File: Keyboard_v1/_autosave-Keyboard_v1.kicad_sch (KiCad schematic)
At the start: 16 parts, among them SW1 SW_Push, U1 ATmega32U4-A, Y1 16MHz

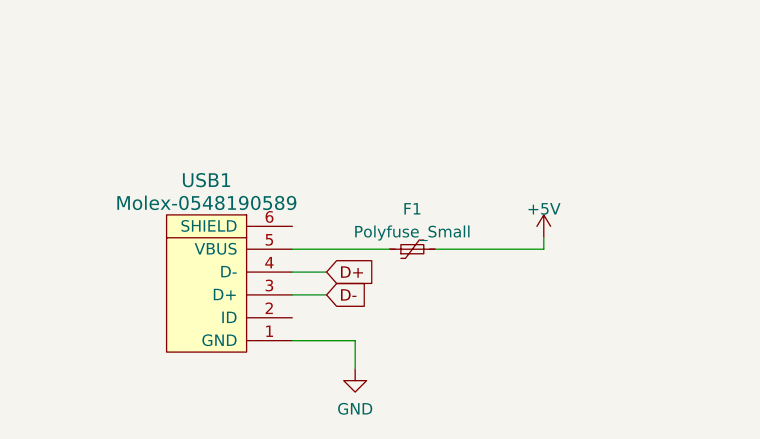
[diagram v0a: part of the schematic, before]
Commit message: routed MCU and key rows
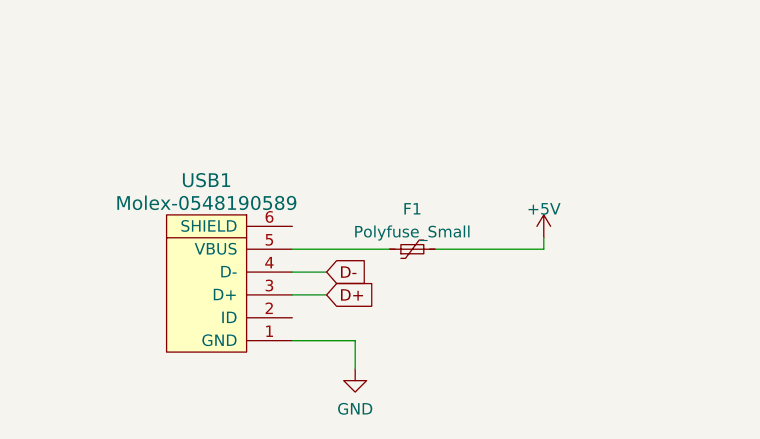
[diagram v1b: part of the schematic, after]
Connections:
- net D+: now also USB1.3 (D+); no longer USB1.4 (D-)
- net D-: now also USB1.4 (D-); no longer USB1.3 (D+)
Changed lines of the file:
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@@
     (effects (font (size 1.27 1.27)) (justify left bottom))
   )
-  (global_label "D+" (shape input) (at 70.485 148.59 0) (fields_autoplaced)
+  (global_label "D+" (shape input) (at 70.485 151.13 0) (fields_autoplaced)
     (effects (font (size 1.27 1.27)) (justify left))
-    (property "Intersheetrefs" "${INTERSHEET_REFS}" (at 76.2332 148.59 0)
+    (property "Intersheetrefs" "${INTERSHEET_REFS}" (at 76.2332 151.13 0)
       (effects (font (size 1.27 1.27)) (justify left) hide)
     )
   )
-  (global_label "D-" (shape input) (at 107.315 78.74 180) (fields_autoplaced)
-    (effects (font (size 1.27 1.27)) (justify right))
-    (property "Intersheetrefs" "${INTERSHEET_REFS}" (at 101.5668 78.74 0)
-      (effects (font (size 1.27 1.27)) (justify right) hide)
-    )
-  )
-  (global_label "D-" (shape input) (at 70.485 151.13 0) (fields_autoplaced)
+  (global_label "D-" (shape input) (at 70.485 148.59 0) (fields_autoplaced)
     (effects (font (size 1.27 1.27)) (justify left))
-    (property "Intersheetrefs" "${INTERSHEET_REFS}" (at 76.2332 151.13 0)
+    (property "Intersheetrefs" "${INTERSHEET_REFS}" (at 76.2332 148.59 0)
       (effects (font (size 1.27 1.27)) (justify left) hide)
     )
@@
       (effects (font (size 1.27 1.27)) (justify right) hide)
     )
+  )
+  (global_label "D-" (shape input) (at 107.315 78.74 180) (fields_autoplaced)
+    (effects (font (size 1.27 1.27)) (justify right))
+    (property "Intersheetrefs" "${INTERSHEET_REFS}" (at 101.5668 78.74 0)
+      (effects (font (size 1.27 1.27)) (justify right) hide)
+    )

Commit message: all rows and cols connected to MCU
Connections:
- net ROW2: now reaches U1.10 (PB2)
- net ROW3: now reaches U1.11 (PB3)
- net COL13: now reaches U1.18 (PD0)
- net COL12: now reaches U1.19 (PD1)
- net ROW4: now reaches U1.20 (PD2)
- net ROW5: now reaches U1.21 (PD3)
- net COL11: now reaches U1.22 (PD5)
- net COL3: now reaches U1.25 (PD4)
- net COL4: now reaches U1.26 (PD6)
- net COL5: now reaches U1.27 (PD7)
- net COL6: now reaches U1.28 (PB4)
- net COL7: now reaches U1.29 (PB5)
- net COL8: now reaches U1.30 (PB6)
- net COL9: now reaches U1.31 (PC6)
- net COL10: now reaches U1.32 (PC7)
- net COL0: now reaches U1.38 (PF5)
- net COL1: now reaches U1.39 (PF4)
- net COL2: now reaches U1.40 (PF1)
- net ROW0: now reaches U1.8 (PB0)
- net ROW1: now reaches U1.9 (PB1)
- no-connect marks 26 -> 6
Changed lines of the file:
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@@
   (junction (at 125.095 60.96) (diameter 0) (color 0 0 0 0)
   )
-  (no_connect (at 175.26 83.82))
   (no_connect (at 175.26 106.68))
   (no_connect (at 144.78 66.04))
-  (no_connect (at 175.26 66.04))
-  (no_connect (at 175.26 96.52))
-  (no_connect (at 175.26 63.5))
   (no_connect (at 175.26 121.92))
-  (no_connect (at 175.26 99.06))
-  (no_connect (at 175.26 116.84))
-  (no_connect (at 175.26 50.8))
-  (no_connect (at 175.26 119.38))
-  (no_connect (at 175.26 58.42))
-  (no_connect (at 175.26 55.88))
-  (no_connect (at 175.26 114.3))
-  (no_connect (at 175.26 53.34))
-  (no_connect (at 175.26 73.66))
-  (no_connect (at 175.26 93.98))
-  (no_connect (at 175.26 81.28))
-  (no_connect (at 175.26 86.36))
   (no_connect (at 175.26 111.76))
-  (no_connect (at 175.26 60.96))
   (no_connect (at 175.26 124.46))
   (no_connect (at 175.26 68.58))
-  (no_connect (at 175.26 88.9))
-  (no_connect (at 175.26 91.44))
-  (no_connect (at 175.26 76.2))
   (wire (pts (xy 162.56 41.91) (xy 162.56 43.18))
     (stroke (width 0) (type default))
@@
     (stroke (width 0) (type default))
   )
-  (wire (pts (xy 182.88 104.14) (xy 182.88 112.395))
+  (wire (pts (xy 183.515 104.14) (xy 183.515 106.045))
     (stroke (width 0) (type default))
   )
@@
     (stroke (width 0) (type default))
   )
-  (wire (pts (xy 181.61 104.14) (xy 182.88 104.14))
+  (wire (pts (xy 181.61 104.14) (xy 183.515 104.14))
     (stroke (width 0) (type default))
   )
@@
     (effects (font (size 1.27 1.27)) (justify left bottom))
   )
+  (global_label "COL4" (shape input) (at 175.26 96.52 0) (fields_autoplaced)
+    (effects (font (size 1.27 1.27)) (justify left))
+    (property "Intersheetrefs" "${INTERSHEET_REFS}" (at 183.0039 96.52 0)
+      (effects (font (size 1.27 1.27)) (justify left) hide)
+    )
+  )
+  (global_label "COL0" (shape input) (at 175.26 119.38 0) (fields_autoplaced)
+    (effects (font (size 1.27 1.27)) (justify left))
+    (property "Intersheetrefs" "${INTERSHEET_REFS}" (at 183.0039 119.38 0)
+      (effects (font (size 1.27 1.27)) (justify left) hide)
+    )
+  )
+  (global_label "COL8" (shape input) (at 175.26 66.04 0) (fields_autoplaced)
+    (effects (font (size 1.27 1.27)) (justify left))
+    (property "Intersheetrefs" "${INTERSHEET_REFS}" (at 183.0039 66.04 0)
+      (effects (font (size 1.27 1.27)) (justify left) hide)
+    )
+  )
+  (global_label "COL10" (shape input) (at 175.26 76.2 0) (fields_autoplaced)
+    (effects (font (size 1.27 1.27)) (justify left))
+    (property "Intersheetrefs" "${INTERSHEET_REFS}" (at 184.2134 76.2 0)
+      (effects (font (size 1.27 1.27)) (justify left) hide)
+    )
+  )
   (global_label "D+" (shape input) (at 70.485 151.13 0) (fields_autoplaced)
     (effects (font (size 1.27 1.27)) (justify left))
@@
     )
   )
+  (global_label "COL12" (shape input) (at 175.26 83.82 0) (fields_autoplaced)
+    (effects (font (size 1.27 1.27)) (justify left))
+    (property "Intersheetrefs" "${INTERSHEET_REFS}" (at 184.2134 83.82 0)
+      (effects (font (size 1.27 1.27)) (justify left) hide)
+    )
+  )
+  (global_label "COL5" (shape input) (at 175.26 99.06 0) (fields_autoplaced)
+    (effects (font (size 1.27 1.27)) (justify left))
+    (property "Intersheetrefs" "${INTERSHEET_REFS}" (at 183.0039 99.06 0)
+      (effects (font (size 1.27 1.27)) (justify left) hide)
+    )
+  )
   (global_label "D-" (shape input) (at 70.485 148.59 0) (fields_autoplaced)
     (effects (font (size 1.27 1.27)) (justify left))
     (property "Intersheetrefs" "${INTERSHEET_REFS}" (at 76.2332 148.59 0)
+      (effects (font (size 1.27 1.27)) (justify left) hide)
+    )
+  )
+  (global_label "ROW0" (shape input) (at 175.26 50.8 0) (fields_autoplaced)
+    (effects (font (size 1.27 1.27)) (justify left))
+    (property "Intersheetrefs" "${INTERSHEET_REFS}" (at 183.4272 50.8 0)
+      (effects (font (size 1.27 1.27)) (justify left) hide)
+    )
+  )
+  (global_label "COL7" (shape input) (at 175.26 63.5 0) (fields_autoplaced)
+    (effects (font (size 1.27 1.27)) (justify left))
+    (property "Intersheetrefs" "${INTERSHEET_REFS}" (at 183.0039 63.5 0)
+      (effects (font (size 1.27 1.27)) (justify left) hide)
+    )
+  )
+  (global_label "ROW2" (shape input) (at 175.26 55.88 0) (fields_autoplaced)
+    (effects (font (size 1.27 1.27)) (justify left))
+    (property "Intersheetrefs" "${INTERSHEET_REFS}" (at 183.4272 55.88 0)
+      (effects (font (size 1.27 1.27)) (justify left) hide)
+    )
+  )
+  (global_label "ROW4" (shape input) (at 175.26 86.36 0) (fields_autoplaced)
+    (effects (font (size 1.27 1.27)) (justify left))
+    (property "Intersheetrefs" "${INTERSHEET_REFS}" (at 183.4272 86.36 0)
+      (effects (font (size 1.27 1.27)) (justify left) hide)
+    )
+  )
+  (global_label "COL13" (shape input) (at 175.26 81.28 0) (fields_autoplaced)
+    (effects (font (size 1.27 1.27)) (justify left))
+    (property "Intersheetrefs" "${INTERSHEET_REFS}" (at 184.2134 81.28 0)
+      (effects (font (size 1.27 1.27)) (justify left) hide)
+    )
+  )
+  (global_label "COL1" (shape input) (at 175.26 116.84 0) (fields_autoplaced)
+    (effects (font (size 1.27 1.27)) (justify left))
+    (property "Intersheetrefs" "${INTERSHEET_REFS}" (at 183.0039 116.84 0)
+      (effects (font (size 1.27 1.27)) (justify left) hide)
+    )
+  )
+  (global_label "COL9" (shape input) (at 175.26 73.66 0) (fields_autoplaced)
+    (effects (font (size 1.27 1.27)) (justify left))
+    (property "Intersheetrefs" "${INTERSHEET_REFS}" (at 183.0039 73.66 0)
+      (effects (font (size 1.27 1.27)) (justify left) hide)
+    )
+  )
+  (global_label "COL3" (shape input) (at 175.26 91.44 0) (fields_autoplaced)
+    (effects (font (size 1.27 1.27)) (justify left))
+    (property "Intersheetrefs" "${INTERSHEET_REFS}" (at 183.0039 91.44 0)
       (effects (font (size 1.27 1.27)) (justify left) hide)
     )
@@
     (property "Intersheetrefs" "${INTERSHEET_REFS}" (at 101.5668 76.2 0)
       (effects (font (size 1.27 1.27)) (justify right) hide)
+    )
+  )
+  (global_label "COL2" (shape input) (at 175.26 114.3 0) (fields_autoplaced)
+    (effects (font (size 1.27 1.27)) (justify left))
+    (property "Intersheetrefs" "${INTERSHEET_REFS}" (at 183.0039 114.3 0)
+      (effects (font (size 1.27 1.27)) (justify left) hide)
+    )
+  )
+  (global_label "ROW1" (shape input) (at 175.26 53.34 0) (fields_autoplaced)
+    (effects (font (size 1.27 1.27)) (justify left))
+    (property "Intersheetrefs" "${INTERSHEET_REFS}" (at 183.4272 53.34 0)
+      (effects (font (size 1.27 1.27)) (justify left) hide)
+    )
+  )
+  (global_label "ROW5" (shape input) (at 175.26 88.9 0) (fields_autoplaced)
+    (effects (font (size 1.27 1.27)) (justify left))
+    (property "Intersheetrefs" "${INTERSHEET_REFS}" (at 183.4272 88.9 0)
+      (effects (font (size 1.27 1.27)) (justify left) hide)
+    )
+  )
+  (global_label "COL6" (shape input) (at 175.26 60.96 0) (fields_autoplaced)
+    (effects (font (size 1.27 1.27)) (justify left))
+    (property "Intersheetrefs" "${INTERSHEET_REFS}" (at 183.0039 60.96 0)
+      (effects (font (size 1.27 1.27)) (justify left) hide)
+    )
+  )
+  (global_label "COL11" (shape input) (at 175.26 93.98 0) (fields_autoplaced)
+    (effects (font (size 1.27 1.27)) (justify left))
+    (property "Intersheetrefs" "${INTERSHEET_REFS}" (at 184.2134 93.98 0)
+      (effects (font (size 1.27 1.27)) (justify left) hide)
+    )
+  )
+  (global_label "ROW3" (shape input) (at 175.26 58.42 0) (fields_autoplaced)
+    (effects (font (size 1.27 1.27)) (justify left))
+    (property "Intersheetrefs" "${INTERSHEET_REFS}" (at 183.4272 58.42 0)
+      (effects (font (size 1.27 1.27)) (justify left) hide)
     )
   )
@@
   )
   (symbol (lib_id "Device:R_Small") (at 179.07 104.14 90) (unit 1)
-    (in_bom yes) (on_board yes) (dnp no) (fields_autoplaced)
-    (property "Reference" "R1" (at 179.07 99.695 90)
+    (in_bom yes) (on_board yes) (dnp no)
+    (property "Reference" "R1" (at 179.07 106.045 90)
       (effects (font (size 1.27 1.27)))
     )
@@
     )
   )
-  (symbol (lib_id "power:GND") (at 182.88 112.395 0) (unit 1)
-    (in_bom yes) (on_board yes) (dnp no) (fields_autoplaced)
-    (property "Reference" "#PWR03" (at 182.88 118.745 0)
-      (effects (font (size 1.27 1.27)) hide)
-    )
-    (property "Value" "GND" (at 182.88 116.84 0)
-      (effects (font (size 1.27 1.27)))
-    )
-    (property "Footprint" "" (at 182.88 112.395 0)
-      (effects (font (size 1.27 1.27)) hide)
-    )
-    (property "Datasheet" "" (at 182.88 112.395 0)
-      (effects (font (size 1.27 1.27)) hide)
-    )
+  (symbol (lib_id "power:GND") (at 183.515 106.045 0) (unit 1)
+    (in_bom yes) (on_board yes) (dnp no) (fields_autoplaced)
+    (property "Reference" "#PWR03" (at 183.515 112.395 0)
+      (effects (font (size 1.27 1.27)) hide)
+    )
+    (property "Value" "GND" (at 183.515 110.49 0)
+      (effects (font (size 1.27 1.27)))
+    )
+    (property "Footprint" "" (at 183.515 106.045 0)
+      (effects (font (size 1.27 1.27)) hide)
+    )
+    (property "Datasheet" "" (at 183.515 106.045 0)
+      (effects (font (size 1.27 1.27)) hide)
+    )
